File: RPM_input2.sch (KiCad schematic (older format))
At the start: 30 parts, among them P38 CONN_1, P39 CONN_1, P40 CONN_1, P41 CONN_1, P42 CONN_1, SW7 SWITCH_INV, U7 LM1815, U8 TL082CN

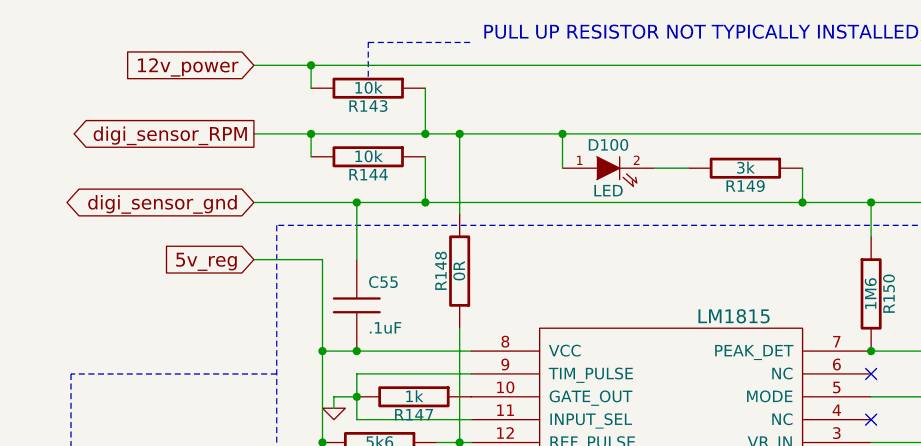
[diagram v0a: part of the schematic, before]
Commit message: DFH mans up a bit. Perhaps usable for something at this point, like making trips to the local store ;)
I connected TA pins to sub circuits, fixed a number if items discussed in the DIYEFI forums. This is it's 21st version, so it was time for it to man up a bit, and become something potentially useful.

Signed-off-by: Jared Harvey <TortiseGIT@jaredharvey.com>
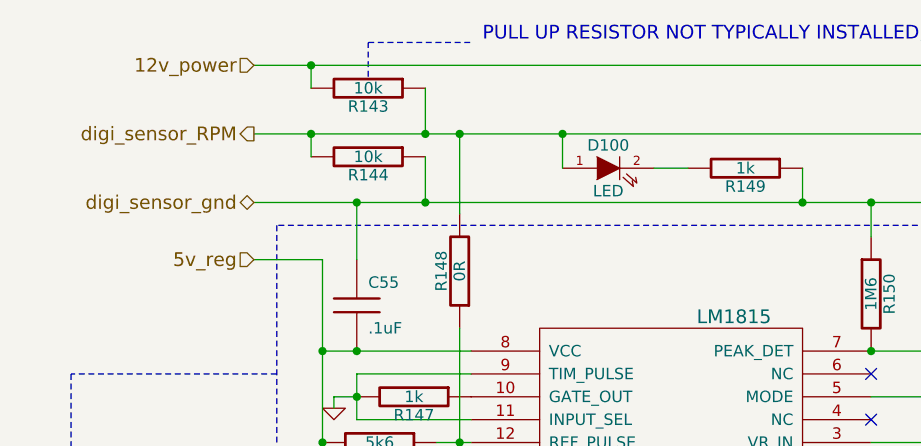
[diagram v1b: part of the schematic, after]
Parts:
- C55: Field10 (none) -> multilayer ceramic; Field11 (none) -> other,more,stuff; Field4 (none) -> newark,97M4164; Field5 (none) -> vendor1, smd w hem; Field6 (none) -> vendor2, thru w hem; Field7 (none) -> vendor2, smd w hem; Field8 (none) -> 50,V; Field9 (none) -> 20,%
- C56: Field10 (none) -> multilayer ceramic; Field11 (none) -> other,more,stuff; Field4 (none) -> newark,93K3279; Field5 (none) -> vendor1, smd w hem; Field6 (none) -> vendor2, thru w hem; Field7 (none) -> vendor2, smd w hem; Field8 (none) -> 100,V; Field9 (none) -> 10,%
- C57: Field10 (none) -> multilayered ceramic; Field11 (none) -> other,more,stuff; Field4 (none) -> newark,36K5919; Field5 (none) -> vendor1, smd w hem; Field6 (none) -> vendor2, thru w hem; Field7 (none) -> vendor2, smd w hem; Field8 (none) -> 100,V; Field9 (none) -> 5,%
- C58: Field10 (none) -> multilayer ceramic; Field11 (none) -> other,more,stuff; Field4 (none) -> newark,89F3212; Field5 (none) -> vendor1, smd w hem; Field6 (none) -> vendor2, thru w hem; Field7 (none) -> vendor2, smd w hem; Field8 (none) -> 50,V; Field9 (none) -> 20,%
- C59: Field10 (none) -> multilayer ceramic; Field11 (none) -> other,more,stuff; Field4 (none) -> newark,97M4158; Field5 (none) -> vendor1, smd w hem; Field6 (none) -> vendor2, thru w hem; Field7 (none) -> vendor2, smd w hem; Field8 (none) -> 10,V; Field9 (none) -> 10,%
- D100: A (none) -> 10mA; V (none) -> 12V; construct (none) -> LED with resistor included; misc (none) -> other,more,stuff; vend1,smd e hem (none) -> newark,; vend2, smd w hem (none) -> digi,; vend2, thru w hem (none) -> digi,; vendor1, thru e hem (none) -> newark,58K2517
- R143, R144: Field10 (none) -> carbon film; Field11 (none) -> other,more,stuff; Field4 (none) -> newark,38k0328; Field5 (none) -> vendor1, smd w hem; Field6 (none) -> vendor2, thru w hem; Field7 (none) -> vendor2, smd w hem; Field8 (none) -> 250,mW; Field9 (none) -> 5,%
- R145, R152: Field10 (none) -> carbon film; Field11 (none) -> other,more,stuff; Field4 (none) -> newark,38K0382; Field5 (none) -> vendor1, smd w hem; Field6 (none) -> vendor2, thru w hem; Field7 (none) -> vendor2, smd w hem; Field8 (none) -> 250,mW; Field9 (none) -> 5,%
- R146: Field10 (none) -> carbon film; Field11 (none) -> other,more,stuff; Field4 (none) -> newark,58K4949; Field5 (none) -> vendor1, smd w hem; Field6 (none) -> vendor2, thru w hem; Field7 (none) -> vendor2, smd w hem; Field8 (none) -> 500,mW; Field9 (none) -> 5,%
- R147: W (none) -> 1/4w; construct (none) -> carbon film; misc (none) -> other,more,stuff; tol (none) -> 5%; vend1,smd e hem (none) -> newark,52K9725; vend2, smd w hem (none) -> digi,CRCW08051K00JNEA; vend2, thru w hem (none) -> digi,OD102J-ND; vendor1, thru e hem (none) -> newark,65K2365
- R148: TOL (none) -> 5%; W (none) -> 1/4W; construct (none) -> carbon film; misc (none) -> other,more,stuff; vend1,smd e hem (none) -> newark,36C9353; vend2, smd w hem (none) -> digi,CRCW08050000ZSTA-ND; vend2, thru w hem (none) -> digi,604HR025E-ND; vendor1, thru e hem (none) -> newark,64K9335
- R149: value 3k -> 1k; W (none) -> 1/4w; construct (none) -> carbon film; misc (none) -> other,more,stuff; tol (none) -> 5%; vend1,smd e hem (none) -> newark,52K9725; vend2, smd w hem (none) -> digi,CRCW08051K00JNEA; vend2, thru w hem (none) -> digi,OD102J-ND; vendor1, thru e hem (none) -> newark,65K2365
- R150: Field10 (none) -> carbon composition; Field11 (none) -> other,more,stuff; Field4 (none) -> newark,73K0277; Field5 (none) -> vendor1, smd w hem; Field6 (none) -> vendor2, thru w hem; Field7 (none) -> vendor2, smd w hem; Field8 (none) -> 250,mW; Field9 (none) -> 5,%
- R151: Field10 (none) -> carbon film; Field11 (none) -> other,more,stuff; Field4 (none) -> newark,58K5022; Field5 (none) -> vendor1, smd w hem; Field6 (none) -> vendor2, thru w hem; Field7 (none) -> vendor2, smd w hem; Field8 (none) -> 250,mW; Field9 (none) -> 5,%
- R153: Field10 (none) -> metal film; Field11 (none) -> other,more,stuff; Field4 (none) -> newark,58K3858; Field5 (none) -> vendor1, smd w hem; Field6 (none) -> vendor2, thru w hem; Field7 (none) -> vendor2, smd w hem; Field8 (none) -> 250,mW; Field9 (none) -> 1,%
- R154: Field10 (none) -> metal film; Field11 (none) -> other,more,stuff; Field4 (none) -> newark,94C4880; Field5 (none) -> vendor1, smd w hem; Field6 (none) -> vendor2, thru w hem; Field7 (none) -> vendor2, smd w hem; Field8 (none) -> 400,mW; Field9 (none) -> 1,%
- R155: Field10 (none) -> metal film; Field11 (none) -> other,more,stuff; Field4 (none) -> newark,71M1054; Field5 (none) -> vendor1, smd w hem; Field6 (none) -> vendor2, thru w hem; Field7 (none) -> vendor2, smd w hem; Field8 (none) -> 500,mW; Field9 (none) -> 1,%
- R156: Field10 (none) -> metal film; Field11 (none) -> other,more,stuff; Field4 (none) -> newark,58K3819; Field5 (none) -> vendor1, smd w hem; Field6 (none) -> vendor2, thru w hem; Field7 (none) -> vendor2, smd w hem; Field8 (none) -> 250,mW; Field9 (none) -> 1,%
- R157: Field10 (none) -> metal film; Field11 (none) -> other,more,stuff; Field4 (none) -> newark,58K3844; Field5 (none) -> vendor1, smd w hem; Field6 (none) -> vendor2, thru w hem; Field7 (none) -> vendor2, smd w hem; Field8 (none) -> 250,mW; Field9 (none) -> 1,%
- R158: Field10 (none) -> metal film; Field11 (none) -> other,more,stuff; Field4 (none) -> newark,58K3797; Field5 (none) -> vendor1, smd w hem; Field6 (none) -> vendor2, thru w hem; Field7 (none) -> vendor2, smd w hem; Field8 (none) -> 250,mW; Field9 (none) -> 1,%
- SW7: Field10 (none) -> x,x; Field11 (none) -> x,x,x; Field4 (none) -> vendor1, thru w hem; Field5 (none) -> vendor1, thru smd w hem; Field6 (none) -> vendor2, thru w hem; Field7 (none) -> vendor2, thru smd w hem; Field8 (none) -> x,x; Field9 (none) -> x,x
- U7: Field10 (none) -> VR RPM chip; Field11 (none) -> x,x,x; Field4 (none) -> newark,41K3517; Field5 (none) -> vendor2, thru e hem; Field6 (none) -> vendor2, thru w hem; Field7 (none) -> newark,41k3517; Field8 (none) -> x,x; Field9 (none) -> x,x
- U8: Field10 (none) -> opamp; Field11 (none) -> other,more,stuff; Field4 (none) -> newark,89K1104; Field5 (none) -> vendor1, smd w hem; Field6 (none) -> digi,497-2213-5-ND; Field7 (none) -> vendor2, smd w hem; Field8 (none) -> x,x; Field9 (none) -> x,x

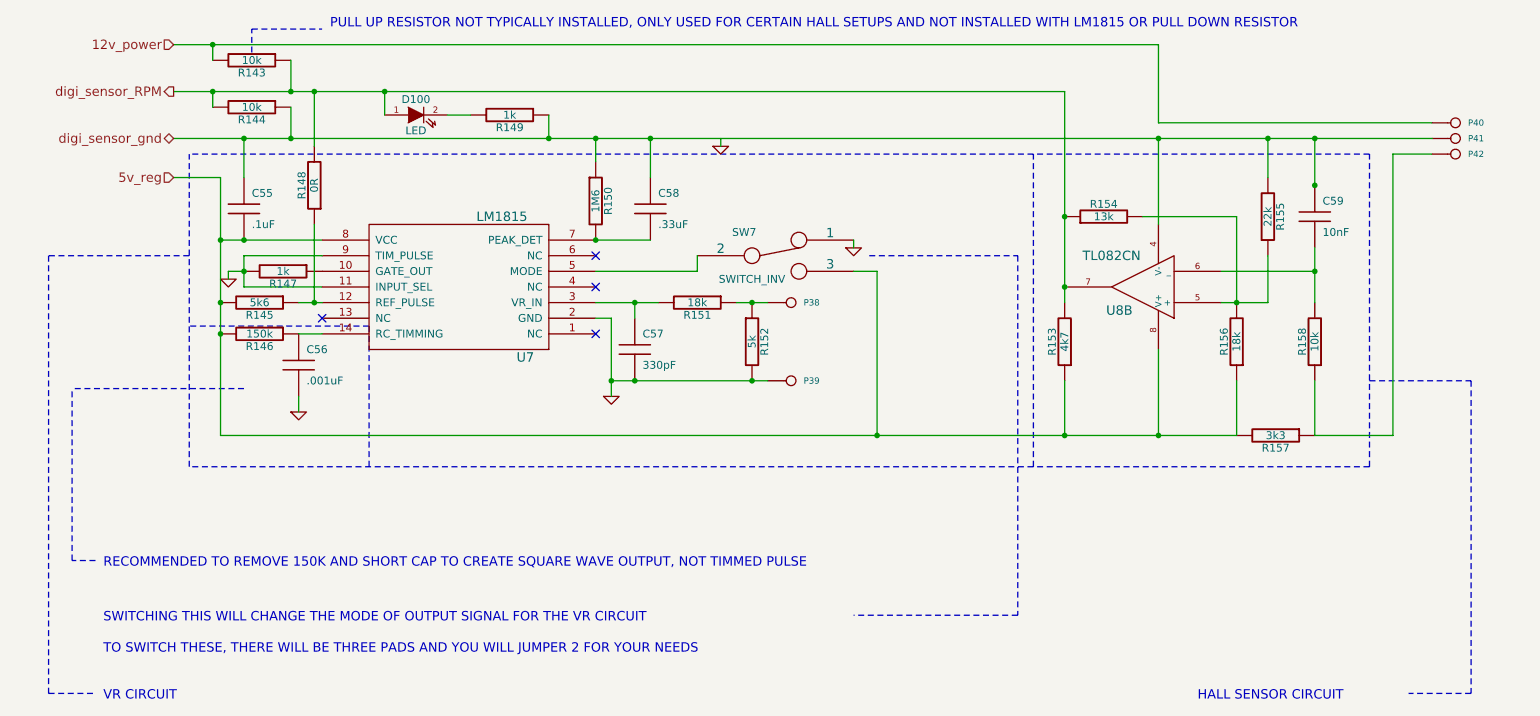
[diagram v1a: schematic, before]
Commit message: Changed from LM chip, to JBPerf VR board.
Signed-off-by: Jared Harvey <TortiseGIT@jaredharvey.com>
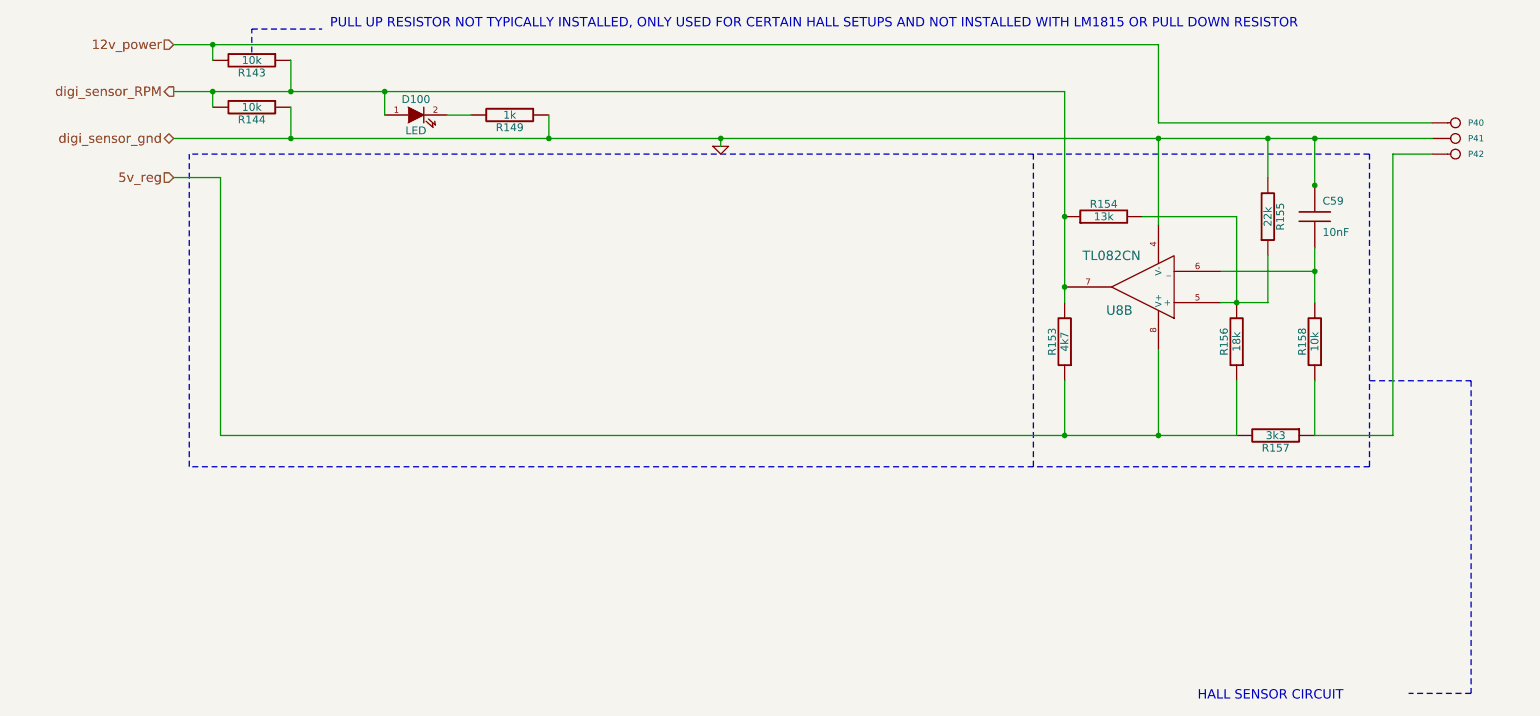
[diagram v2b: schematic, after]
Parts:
- removed C55: .1uF, C1V7, symbol C
- removed C56: .001uF, C1V7, symbol C
- removed C57: 330pF, C1V7, symbol C
- removed C58: .33uF, C1V7, symbol C
- removed P38, P39: CONN_1, 1PIN, symbol CONN_1
- removed R145: 5k6, R4-SM0805, symbol R
- removed R146: 150k, R4-SM0805, symbol R
- removed R147: 1k, R4-SM0805, symbol R
- removed R148: 0R, R4-SM0805, symbol R
- removed R150: 1M6, R4-SM0805, symbol R
- removed R151: 18k, R4-SM0805, symbol R
- removed R152: 5k, R4-SM0805, symbol R
- removed SW7: SWITCH_INV, SIL-3, symbol SWITCH_INV
- removed U7: LM1815, SO14E, symbol LM1815
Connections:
- net digi_sensor_gnd is gone; now on net GND: C59.1, P41.1, R144.1, R149.1, R155.2, U8.4 (V-)
- no-connect marks 4 -> 0
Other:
- note removed: "RECOMMENDED TO REMOVE 150K AND SHORT CAP TO CREATE SQUARE WAVE OUTPUT, NOT TIMMED PULSE"
- note removed: "SWITCHING THIS WILL CHANGE THE MODE OF OUTPUT SIGNAL FOR THE VR CIRCUIT"
- note removed: "TO SWITCH THESE, THERE WILL BE THREE PADS AND YOU WILL JUMPER 2 FOR YOUR NEEDS"
- note removed: "VR CIRCUIT"
